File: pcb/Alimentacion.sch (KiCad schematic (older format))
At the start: 1 part

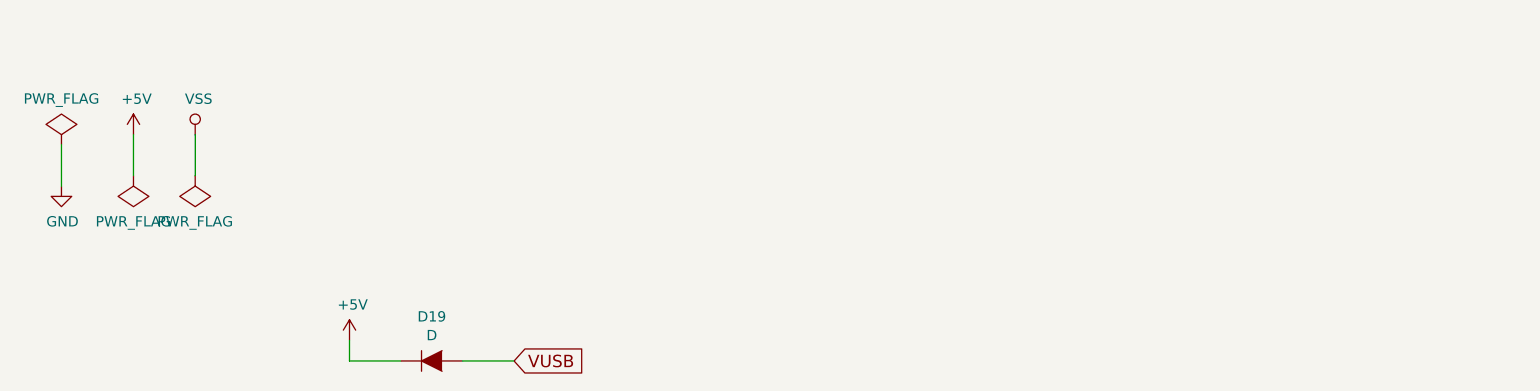
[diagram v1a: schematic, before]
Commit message: finalizada realizacion de esquema
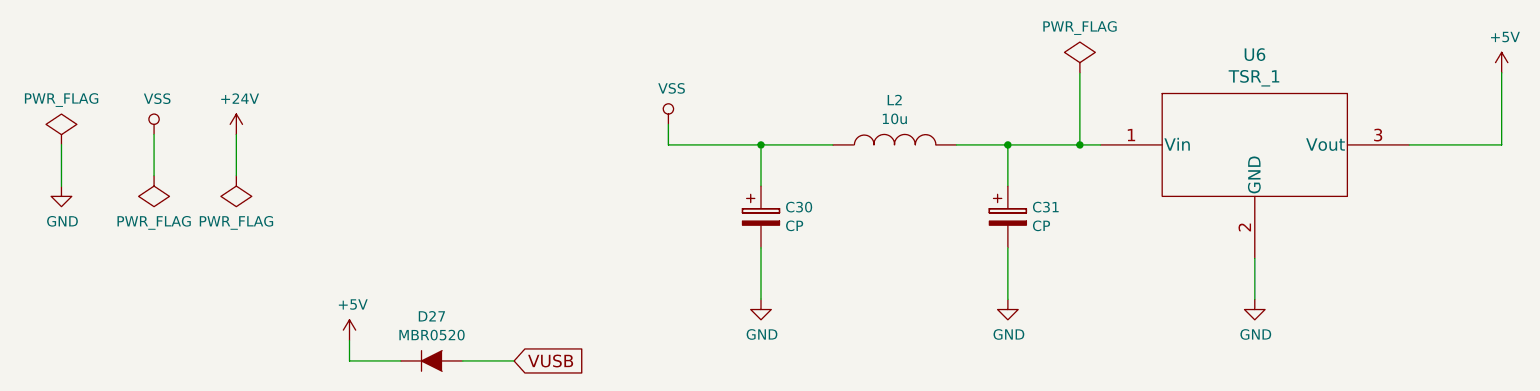
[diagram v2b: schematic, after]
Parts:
- added C30, C31: CP, symbol CP
- added L2: 10u, symbol L
- added U6: TSR_1, symbol TSR_1
- D27: renamed from D19; value D -> MBR0520; Fabricante (none) -> FAIRCHILD SEMICONDUCTOR; Provedor (none) -> tme; Ref (none) -> MBR0520L; Ref_Proveedor (none) -> MBR0520L
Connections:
- net +5V: now also U6.3 (Vout)
- net GND: now also C30.2, C31.2, U6.2 (GND)
- net VSS: now also C30.1, L2.1
- new net: C31.1, L2.2, U6.1 (Vin)
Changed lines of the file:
@@
 LIBS:connector
 LIBS:Opamp
+LIBS:Traco
 LIBS:ATMEGA328_Motor_Board-cache
 EELAYER 25 0
@@
 $EndDescr
 $Comp
-L GND #PWR053
+L GND #PWR061
 U 1 1 5768B46A
 P 1550 2150
-F 0 "#PWR053" H 1550 1900 50  0001 C CNN
+F 0 "#PWR061" H 1550 1900 50  0001 C CNN
 F 1 "GND" H 1555 1977 50  0000 C CNN
 F 2 "" H 1550 2150 50  0000 C CNN
@@
 $EndComp
 $Comp
-L PWR_FLAG #FLG054
+L PWR_FLAG #FLG062
 U 1 1 5768B47E
 P 1550 1950
-F 0 "#FLG054" H 1550 2045 50  0001 C CNN
+F 0 "#FLG062" H 1550 2045 50  0001 C CNN
 F 1 "PWR_FLAG" H 1550 2174 50  0000 C CNN
 F 2 "" H 1550 1950 50  0000 C CNN
@@
 	1550 1950 1550 2150
 $Comp
-L PWR_FLAG #FLG055
-U 1 1 5768B492
-P 1900 2100
-F 0 "#FLG055" H 1900 2195 50  0001 C CNN
-F 1 "PWR_FLAG" H 1900 2323 50  0000 C CNN
-F 2 "" H 1900 2100 50  0000 C CNN
-F 3 "" H 1900 2100 50  0000 C CNN
-	1    1900 2100
+L VSS #PWR063
+U 1 1 576A7AE8
+P 2000 1900
+F 0 "#PWR063" H 2000 1750 50  0001 C CNN
+F 1 "VSS" H 2017 2073 50  0000 C CNN
+F 2 "" H 2000 1900 50  0000 C CNN
+F 3 "" H 2000 1900 50  0000 C CNN
+	1    2000 1900
+	1    0    0    -1
+$EndComp
+$Comp
+L PWR_FLAG #FLG064
+U 1 1 576A7AFA
+P 2000 2100
+F 0 "#FLG064" H 2000 2195 50  0001 C CNN
+F 1 "PWR_FLAG" H 2000 2323 50  0000 C CNN
+F 2 "" H 2000 2100 50  0000 C CNN
+F 3 "" H 2000 2100 50  0000 C CNN
+	1    2000 2100
 	-1   0    0    1
 $EndComp
-$Comp
-L +5V #PWR056
-U 1 1 5768B49F
-P 1900 1900
-F 0 "#PWR056" H 1900 1750 50  0001 C CNN
-F 1 "+5V" H 1915 2073 50  0000 C CNN
-F 2 "" H 1900 1900 50  0000 C CNN
-F 3 "" H 1900 1900 50  0000 C CNN
-	1    1900 1900
-	1    0    0    -1
-$EndComp
-Wire Wire Line
-	1900 1900 1900 2100
-$Comp
-L VSS #PWR057
-U 1 1 576A7AE8
-P 2200 1900
-F 0 "#PWR057" H 2200 1750 50  0001 C CNN
-F 1 "VSS" H 2217 2073 50  0000 C CNN
-F 2 "" H 2200 1900 50  0000 C CNN
-F 3 "" H 2200 1900 50  0000 C CNN
-	1    2200 1900
-	1    0    0    -1
-$EndComp
-$Comp
-L PWR_FLAG #FLG058
-U 1 1 576A7AFA
-P 2200 2100
-F 0 "#FLG058" H 2200 2195 50  0001 C CNN
-F 1 "PWR_FLAG" H 2200 2323 50  0000 C CNN
-F 2 "" H 2200 2100 50  0000 C CNN
-F 3 "" H 2200 2100 50  0000 C CNN
-	1    2200 2100
-	-1   0    0    1
-$EndComp
-Wire Wire Line
-	2200 2100 2200 1900
-$Comp
-L D D19
+Wire Wire Line
+	2000 2100 2000 1900
+$Comp
+L D D27
 U 1 1 576A8276
 P 3350 3000
-F 0 "D19" H 3350 3215 50  0000 C CNN
-F 1 "D" H 3350 3124 50  0000 C CNN
+F 0 "D27" H 3350 3215 50  0000 C CNN
+F 1 "MBR0520" H 3350 3124 50  0000 C CNN
 F 2 "" H 3350 3000 50  0000 C CNN
 F 3 "" H 3350 3000 50  0000 C CNN
-F 4 "~" H 2200 2000 60  0001 C CNN "Fabricante"
-F 5 "~" H 2200 2000 60  0001 C CNN "Ref"
+F 4 "FAIRCHILD SEMICONDUCTOR" H 2200 2000 60  0001 C CNN "Fabricante"
+F 5 "MBR0520L" H 2200 2000 60  0001 C CNN "Ref"
 F 6 "~" H 2200 2000 60  0001 C CNN "Potencia"
 F 7 "~" H 2200 2000 60  0001 C CNN "Tolerancia"
-F 8 "~" H 2200 2000 60  0001 C CNN "Provedor"
-F 9 "~" H 2200 2000 60  0001 C CNN "Ref_Proveedor"
+F 8 "tme" H 2200 2000 60  0001 C CNN "Provedor"
+F 9 "MBR0520L" H 2200 2000 60  0001 C CNN "Ref_Proveedor"
 	1    3350 3000
 	1    0    0    -1
@@
 	2950 3000 2950 2900
 $Comp
-L +5V #PWR059
+L +5V #PWR065
 U 1 1 576A82A8
 P 2950 2900
-F 0 "#PWR059" H 2950 2750 50  0001 C CNN
+F 0 "#PWR065" H 2950 2750 50  0001 C CNN
 F 1 "+5V" H 2965 3073 50  0000 C CNN
 F 2 "" H 2950 2900 50  0000 C CNN
@@
 	1    0    0    -1
 $EndComp
+$Comp
+L TSR_1 U6
+U 1 1 576F145A
+P 7350 2300
+F 0 "U6" H 7350 3087 60  0000 C CNN
+F 1 "TSR_1" H 7350 2981 60  0000 C CNN
+F 2 "" H 7350 2300 60  0000 C CNN
+F 3 "" H 7350 2300 60  0000 C CNN
+F 4 "TRACOPOWER" H 7350 2300 60  0001 C CNN "Fabricante"
+F 5 "TSR 1-2450" H 7350 2300 60  0001 C CNN "Ref"
+F 6 "~" H 7350 2300 60  0001 C CNN "Potencia"
+F 7 "~" H 7350 2300 60  0001 C CNN "Tolerancia"
+F 8 "rs" H 7350 2300 60  0001 C CNN "Provedor"
+F 9 "666-4379" H 7350 2300 60  0001 C CNN "Ref_Proveedor"
+	1    7350 2300
+	1    0    0    -1
+$EndComp
+$Comp
+L L L2
+U 1 1 576F1664
+P 5600 1950
+F 0 "L2" V 5816 1950 50  0000 C CNN
+F 1 "10u" V 5725 1950 50  0000 C CNN
+F 2 "" H 5600 1950 50  0000 C CNN
+F 3 "" H 5600 1950 50  0000 C CNN
+F 4 "FERROCORE" H 5600 1950 60  0001 C CNN "Fabricante"
+F 5 "DER0705-10" H 5600 1950 60  0001 C CNN "Ref"
+F 6 "~" H 5600 1950 60  0001 C CNN "Potencia"
+F 7 "~" H 5600 1950 60  0001 C CNN "Tolerancia"
+F 8 "tme" H 5600 1950 60  0001 C CNN "Provedor"
+F 9 "DER0705-10" H 5600 1950 60  0001 C CNN "Ref_Proveedor"
+	1    5600 1950
+	0    -1   -1   0
+$EndComp
+Wire Wire Line
+	5900 1950 6600 1950
+Wire Wire Line
+	6150 1950 6150 2150
+Connection ~ 6150 1950
+Wire Wire Line
+	7350 2500 7350 2700
+$Comp
+L GND #PWR066
+U 1 1 576F176B
+P 7350 2700
+F 0 "#PWR066" H 7350 2450 50  0001 C CNN
+F 1 "GND" H 7355 2527 50  0000 C CNN
+F 2 "" H 7350 2700 50  0000 C CNN
+F 3 "" H 7350 2700 50  0000 C CNN
+	1    7350 2700
+	1    0    0    -1
+$EndComp
+$Comp
+L GND #PWR067
+U 1 1 576F178C
+P 6150 2700
+F 0 "#PWR067" H 6150 2450 50  0001 C CNN
+F 1 "GND" H 6155 2527 50  0000 C CNN
+F 2 "" H 6150 2700 50  0000 C CNN
+F 3 "" H 6150 2700 50  0000 C CNN
+	1    6150 2700
+	1    0    0    -1
+$EndComp
+$Comp
+L GND #PWR068
+U 1 1 576F17A6
+P 4950 2700
+F 0 "#PWR068" H 4950 2450 50  0001 C CNN
+F 1 "GND" H 4955 2527 50  0000 C CNN
+F 2 "" H 4950 2700 50  0000 C CNN
+F 3 "" H 4950 2700 50  0000 C CNN
+	1    4950 2700
+	1    0    0    -1
+$EndComp
+Wire Wire Line
+	4950 2450 4950 2700
+Wire Wire Line
+	6150 2700 6150 2450
+Wire Wire Line
+	5300 1950 4500 1950
+Wire Wire Line
+	4950 2150 4950 1950
+Connection ~ 4950 1950
+Wire Wire Line
+	8100 1950 8550 1950
+Wire Wire Line
+	8550 1950 8550 1600
+$Comp
+L +5V #PWR069
+U 1 1 576F18D7
+P 8550 1600
+F 0 "#PWR069" H 8550 1450 50  0001 C CNN
+F 1 "+5V" H 8565 1773 50  0000 C CNN
+F 2 "" H 8550 1600 50  0000 C CNN
+F 3 "" H 8550 1600 50  0000 C CNN
+	1    8550 1600
+	1    0    0    -1
+$EndComp
+$Comp
+L CP C31
+U 1 1 576F1971
+P 6150 2300
+F 0 "C31" H 6268 2346 50  0000 L CNN
+F 1 "CP" H 6268 2255 50  0000 L CNN
+F 2 "" H 6188 2150 50  0000 C CNN
+F 3 "" H 6150 2300 50  0000 C CNN
+	1    6150 2300
+	1    0    0    -1
+$EndComp
+$Comp
+L CP C30
+U 1 1 576F199B
+P 4950 2300
+F 0 "C30" H 5068 2346 50  0000 L CNN
+F 1 "CP" H 5068 2255 50  0000 L CNN
+F 2 "" H 4988 2150 50  0000 C CNN
+F 3 "" H 4950 2300 50  0000 C CNN
+	1    4950 2300
+	1    0    0    -1
+$EndComp
 Text GLabel 3750 3000 2    60   Input ~ 0
 VUSB
+$Comp
+L VSS #PWR070
+U 1 1 576F3D62
+P 4500 1850
+F 0 "#PWR070" H 4500 1700 50  0001 C CNN
+F 1 "VSS" H 4517 2023 50  0000 C CNN
+F 2 "" H 4500 1850 50  0000 C CNN
+F 3 "" H 4500 1850 50  0000 C CNN
+	1    4500 1850
+	1    0    0    -1
+$EndComp
+Wire Wire Line
+	4500 1950 4500 1850
+$Comp
+L PWR_FLAG #FLG071
+U 1 1 576F3DE8
+P 6500 1600
+F 0 "#FLG071" H 6500 1695 50  0001 C CNN
+F 1 "PWR_FLAG" H 6500 1824 50  0000 C CNN
+F 2 "" H 6500 1600 50  0000 C CNN
+F 3 "" H 6500 1600 50  0000 C CNN
+	1    6500 1600
+	1    0    0    -1
+$EndComp
+Wire Wire Line
+	6500 1600 6500 1950
+Connection ~ 6500 1950
+$Comp
+L +24V #PWR072
+U 1 1 576F9726
+P 2400 1900
+F 0 "#PWR072" H 2400 1750 50  0001 C CNN
+F 1 "+24V" H 2415 2073 50  0000 C CNN
+F 2 "" H 2400 1900 50  0000 C CNN
+F 3 "" H 2400 1900 50  0000 C CNN
+	1    2400 1900
+	1    0    0    -1
+$EndComp
+$Comp
+L PWR_FLAG #FLG073
+U 1 1 576F9747
+P 2400 2100
+F 0 "#FLG073" H 2400 2195 50  0001 C CNN
+F 1 "PWR_FLAG" H 2400 2323 50  0000 C CNN
+F 2 "" H 2400 2100 50  0000 C CNN
+F 3 "" H 2400 2100 50  0000 C CNN
+	1    2400 2100
+	-1   0    0    1
+$EndComp
+Wire Wire Line
+	2400 2100 2400 1900
 $EndSCHEMATC

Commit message: asociacion de huellas a resistencias y condensadores
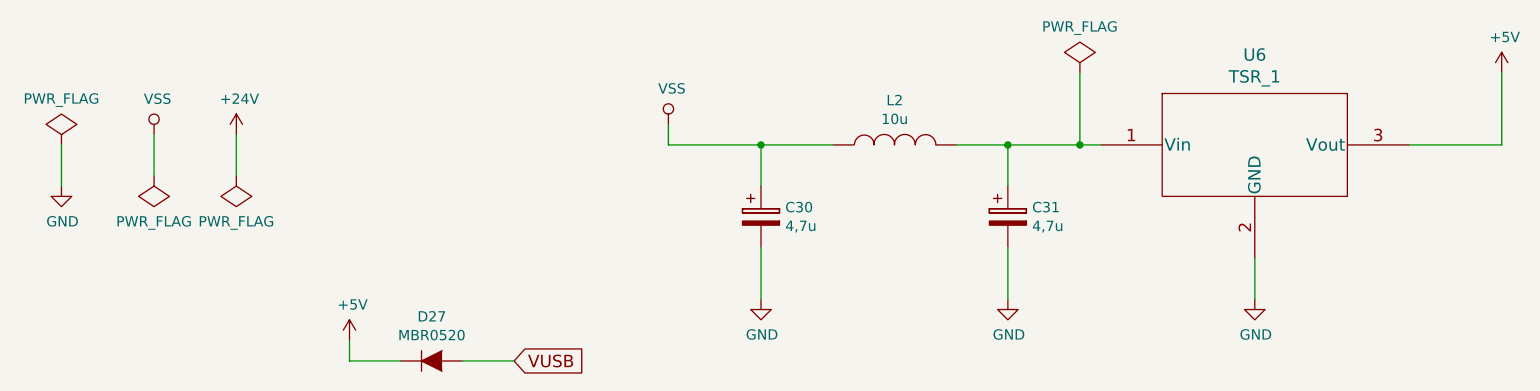
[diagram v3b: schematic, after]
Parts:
- C30, C31: value CP -> 4,7u; footprint (none) -> Capacitors_Tantalum_SMD:TantalC_SizeD_EIA-7343_Wave; Fabricante (none) -> AVX; Provedor (none) -> tme; Ref (none) -> TAJD475K050R; Ref_Proveedor (none) -> TAJD475K050R
- U6: footprint (none) -> Traco:TSR-1
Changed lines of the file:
@@
 F 0 "D27" H 3350 3215 50  0000 C CNN
 F 1 "MBR0520" H 3350 3124 50  0000 C CNN
-F 2 "" H 3350 3000 50  0000 C CNN
+F 2 "" H 3350 3000 50  0001 C CNN
 F 3 "" H 3350 3000 50  0000 C CNN
 F 4 "FAIRCHILD SEMICONDUCTOR" H 2200 2000 60  0001 C CNN "Fabricante"
@@
 F 0 "U6" H 7350 3087 60  0000 C CNN
 F 1 "TSR_1" H 7350 2981 60  0000 C CNN
-F 2 "" H 7350 2300 60  0000 C CNN
+F 2 "Traco:TSR-1" H 7350 2300 60  0001 C CNN
 F 3 "" H 7350 2300 60  0000 C CNN
 F 4 "TRACOPOWER" H 7350 2300 60  0001 C CNN "Fabricante"
@@
 F 0 "L2" V 5816 1950 50  0000 C CNN
 F 1 "10u" V 5725 1950 50  0000 C CNN
-F 2 "" H 5600 1950 50  0000 C CNN
+F 2 "" H 5600 1950 50  0001 C CNN
 F 3 "" H 5600 1950 50  0000 C CNN
 F 4 "FERROCORE" H 5600 1950 60  0001 C CNN "Fabricante"
@@
 P 6150 2300
 F 0 "C31" H 6268 2346 50  0000 L CNN
-F 1 "CP" H 6268 2255 50  0000 L CNN
-F 2 "" H 6188 2150 50  0000 C CNN
+F 1 "4,7u" H 6268 2255 50  0000 L CNN
+F 2 "Capacitors_Tantalum_SMD:TantalC_SizeD_EIA-7343_Wave" H 6188 2150 50  0001 C CNN
 F 3 "" H 6150 2300 50  0000 C CNN
+F 4 "AVX" H 6150 2300 60  0001 C CNN "Fabricante"
+F 5 "TAJD475K050R" H 6150 2300 60  0001 C CNN "Ref"
+F 6 "~" H 6150 2300 60  0001 C CNN "Potencia"
+F 7 "~" H 6150 2300 60  0001 C CNN "Tolerancia"
+F 8 "tme" H 6150 2300 60  0001 C CNN "Provedor"
+F 9 "TAJD475K050R" H 6150 2300 60  0001 C CNN "Ref_Proveedor"
 	1    6150 2300
 	1    0    0    -1
@@
 P 4950 2300
 F 0 "C30" H 5068 2346 50  0000 L CNN
-F 1 "CP" H 5068 2255 50  0000 L CNN
-F 2 "" H 4988 2150 50  0000 C CNN
+F 1 "4,7u" H 5068 2255 50  0000 L CNN
+F 2 "Capacitors_Tantalum_SMD:TantalC_SizeD_EIA-7343_Wave" H 4988 2150 50  0001 C CNN
 F 3 "" H 4950 2300 50  0000 C CNN
+F 4 "AVX" H 4950 2300 60  0001 C CNN "Fabricante"
+F 5 "TAJD475K050R" H 4950 2300 60  0001 C CNN "Ref"
+F 6 "~" H 4950 2300 60  0001 C CNN "Potencia"
+F 7 "~" H 4950 2300 60  0001 C CNN "Tolerancia"
+F 8 "tme" H 4950 2300 60  0001 C CNN "Provedor"
+F 9 "TAJD475K050R" H 4950 2300 60  0001 C CNN "Ref_Proveedor"
 	1    4950 2300
 	1    0    0    -1

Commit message: añadidas asociaciones de condensadores y led
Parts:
- C30, C31: footprint Capacitors_Tantalum_SMD:TantalC_SizeD_EIA-7343_Wave -> Condensadores:TantalC_SizeD_EIA-7343_Wave
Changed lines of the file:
@@
 F 0 "C31" H 6268 2346 50  0000 L CNN
 F 1 "4,7u" H 6268 2255 50  0000 L CNN
-F 2 "Capacitors_Tantalum_SMD:TantalC_SizeD_EIA-7343_Wave" H 6188 2150 50  0001 C CNN
+F 2 "Condensadores:TantalC_SizeD_EIA-7343_Wave" H 6188 2150 50  0001 C CNN
 F 3 "" H 6150 2300 50  0000 C CNN
 F 4 "AVX" H 6150 2300 60  0001 C CNN "Fabricante"
@@
 F 0 "C30" H 5068 2346 50  0000 L CNN
 F 1 "4,7u" H 5068 2255 50  0000 L CNN
-F 2 "Capacitors_Tantalum_SMD:TantalC_SizeD_EIA-7343_Wave" H 4988 2150 50  0001 C CNN
+F 2 "Condensadores:TantalC_SizeD_EIA-7343_Wave" H 4988 2150 50  0001 C CNN
 F 3 "" H 4950 2300 50  0000 C CNN
 F 4 "AVX" H 4950 2300 60  0001 C CNN "Fabricante"

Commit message: añadidas huellas para los borneros
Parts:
- D27: footprint (none) -> Diodos:SOD-123
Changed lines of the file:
@@
 F 0 "D27" H 3350 3215 50  0000 C CNN
 F 1 "MBR0520" H 3350 3124 50  0000 C CNN
-F 2 "" H 3350 3000 50  0001 C CNN
+F 2 "Diodos:SOD-123" H 3350 3000 50  0001 C CNN
 F 3 "" H 3350 3000 50  0000 C CNN
 F 4 "FAIRCHILD SEMICONDUCTOR" H 2200 2000 60  0001 C CNN "Fabricante"

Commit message: añadida huella para choke alimentacion
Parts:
- C30, C31: footprint Condensadores:TantalC_SizeD_EIA-7343_Wave -> Condensadores:TantalC_SizeC_EIA-6032_Wave; Ref TAJD475K050R -> TAJC475K050R; Ref_Proveedor TAJD475K050R -> TAJC475K050R
- L2: footprint (none) -> Magneticos:FERROCORE_SMD_0703
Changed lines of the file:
@@
 F 0 "L2" V 5816 1950 50  0000 C CNN
 F 1 "10u" V 5725 1950 50  0000 C CNN
-F 2 "" H 5600 1950 50  0001 C CNN
+F 2 "Magneticos:FERROCORE_SMD_0703" H 5600 1950 50  0001 C CNN
 F 3 "" H 5600 1950 50  0000 C CNN
 F 4 "FERROCORE" H 5600 1950 60  0001 C CNN "Fabricante"
@@
 F 0 "C31" H 6268 2346 50  0000 L CNN
 F 1 "4,7u" H 6268 2255 50  0000 L CNN
-F 2 "Condensadores:TantalC_SizeD_EIA-7343_Wave" H 6188 2150 50  0001 C CNN
+F 2 "Condensadores:TantalC_SizeC_EIA-6032_Wave" H 6188 2150 50  0001 C CNN
 F 3 "" H 6150 2300 50  0000 C CNN
 F 4 "AVX" H 6150 2300 60  0001 C CNN "Fabricante"
-F 5 "TAJD475K050R" H 6150 2300 60  0001 C CNN "Ref"
+F 5 "TAJC475K050R" H 6150 2300 60  0001 C CNN "Ref"
 F 6 "~" H 6150 2300 60  0001 C CNN "Potencia"
 F 7 "~" H 6150 2300 60  0001 C CNN "Tolerancia"
 F 8 "tme" H 6150 2300 60  0001 C CNN "Provedor"
-F 9 "TAJD475K050R" H 6150 2300 60  0001 C CNN "Ref_Proveedor"
+F 9 "TAJC475K050R" H 6150 2300 60  0001 C CNN "Ref_Proveedor"
 	1    6150 2300
 	1    0    0    -1
@@
 F 0 "C30" H 5068 2346 50  0000 L CNN
 F 1 "4,7u" H 5068 2255 50  0000 L CNN
-F 2 "Condensadores:TantalC_SizeD_EIA-7343_Wave" H 4988 2150 50  0001 C CNN
+F 2 "Condensadores:TantalC_SizeC_EIA-6032_Wave" H 4988 2150 50  0001 C CNN
 F 3 "" H 4950 2300 50  0000 C CNN
 F 4 "AVX" H 4950 2300 60  0001 C CNN "Fabricante"
-F 5 "TAJD475K050R" H 4950 2300 60  0001 C CNN "Ref"
+F 5 "TAJC475K050R" H 4950 2300 60  0001 C CNN "Ref"
 F 6 "~" H 4950 2300 60  0001 C CNN "Potencia"
 F 7 "~" H 4950 2300 60  0001 C CNN "Tolerancia"
 F 8 "tme" H 4950 2300 60  0001 C CNN "Provedor"
-F 9 "TAJD475K050R" H 4950 2300 60  0001 C CNN "Ref_Proveedor"
+F 9 "TAJC475K050R" H 4950 2300 60  0001 C CNN "Ref_Proveedor"
 	1    4950 2300
 	1    0    0    -1

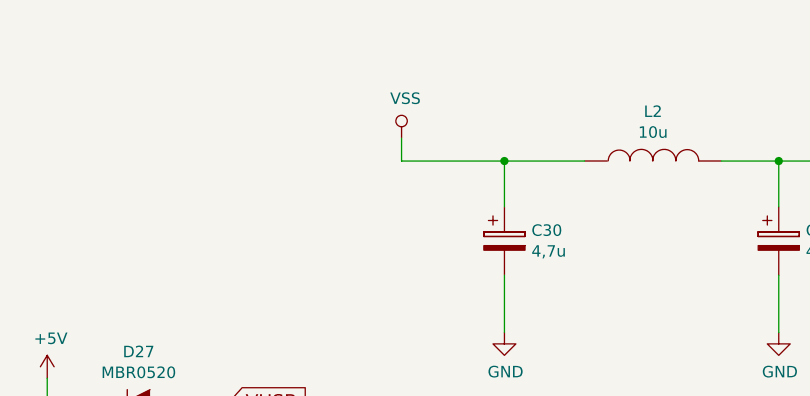
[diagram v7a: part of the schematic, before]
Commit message: comienzo a ordenar paquetes y rutado de potencia
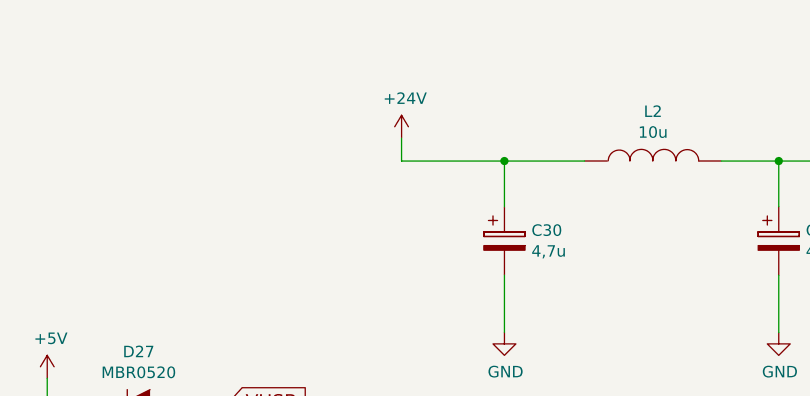
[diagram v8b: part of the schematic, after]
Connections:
- net +24V: now also C30.1, L2.1
- net VSS: no longer C30.1, L2.1
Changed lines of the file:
@@
 Text GLabel 3750 3000 2    60   Input ~ 0
 VUSB
-$Comp
-L VSS #PWR070
-U 1 1 576F3D62
-P 4500 1850
-F 0 "#PWR070" H 4500 1700 50  0001 C CNN
-F 1 "VSS" H 4517 2023 50  0000 C CNN
-F 2 "" H 4500 1850 50  0000 C CNN
-F 3 "" H 4500 1850 50  0000 C CNN
-	1    4500 1850
-	1    0    0    -1
-$EndComp
 Wire Wire Line
 	4500 1950 4500 1850
 $Comp
-L PWR_FLAG #FLG071
+L PWR_FLAG #FLG070
 U 1 1 576F3DE8
 P 6500 1600
-F 0 "#FLG071" H 6500 1695 50  0001 C CNN
+F 0 "#FLG070" H 6500 1695 50  0001 C CNN
 F 1 "PWR_FLAG" H 6500 1824 50  0000 C CNN
 F 2 "" H 6500 1600 50  0000 C CNN
@@
 Connection ~ 6500 1950
 $Comp
-L +24V #PWR072
+L +24V #PWR071
 U 1 1 576F9726
 P 2400 1900
-F 0 "#PWR072" H 2400 1750 50  0001 C CNN
+F 0 "#PWR071" H 2400 1750 50  0001 C CNN
 F 1 "+24V" H 2415 2073 50  0000 C CNN
 F 2 "" H 2400 1900 50  0000 C CNN
@@
 $EndComp
 $Comp
-L PWR_FLAG #FLG073
+L PWR_FLAG #FLG072
 U 1 1 576F9747
 P 2400 2100
-F 0 "#FLG073" H 2400 2195 50  0001 C CNN
+F 0 "#FLG072" H 2400 2195 50  0001 C CNN
 F 1 "PWR_FLAG" H 2400 2323 50  0000 C CNN
 F 2 "" H 2400 2100 50  0000 C CNN
@@
 Wire Wire Line
 	2400 2100 2400 1900
+$Comp
+L +24V #PWR073
+U 1 1 5786CF27
+P 4500 1850
+F 0 "#PWR073" H 4500 1700 50  0001 C CNN
+F 1 "+24V" H 4515 2023 50  0000 C CNN
+F 2 "" H 4500 1850 50  0000 C CNN
+F 3 "" H 4500 1850 50  0000 C CNN
+	1    4500 1850
+	1    0    0    -1
+$EndComp
 $EndSCHEMATC
